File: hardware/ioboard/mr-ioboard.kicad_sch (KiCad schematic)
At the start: 116 parts, among them J1 Conn_01x40_Shielded, J2 USB_C_Receptacle_USB2.0, J3 Conn_01x06, J4 Micro_SD_Card_Det, J5 Conn_01x04, Q1 2N7002, SW1 SW_Push, U1 TPS62822, U10 F1C200S, U2 TPS56637, U3 TPD2E2U06, U4 DS90C363, U5 TPD2E2U06, U6 LD3985M28R_SOT23, U7 TPS62822, U8 FUSB302BMPX, U9 TPD2E2U06, Y1 24MHz

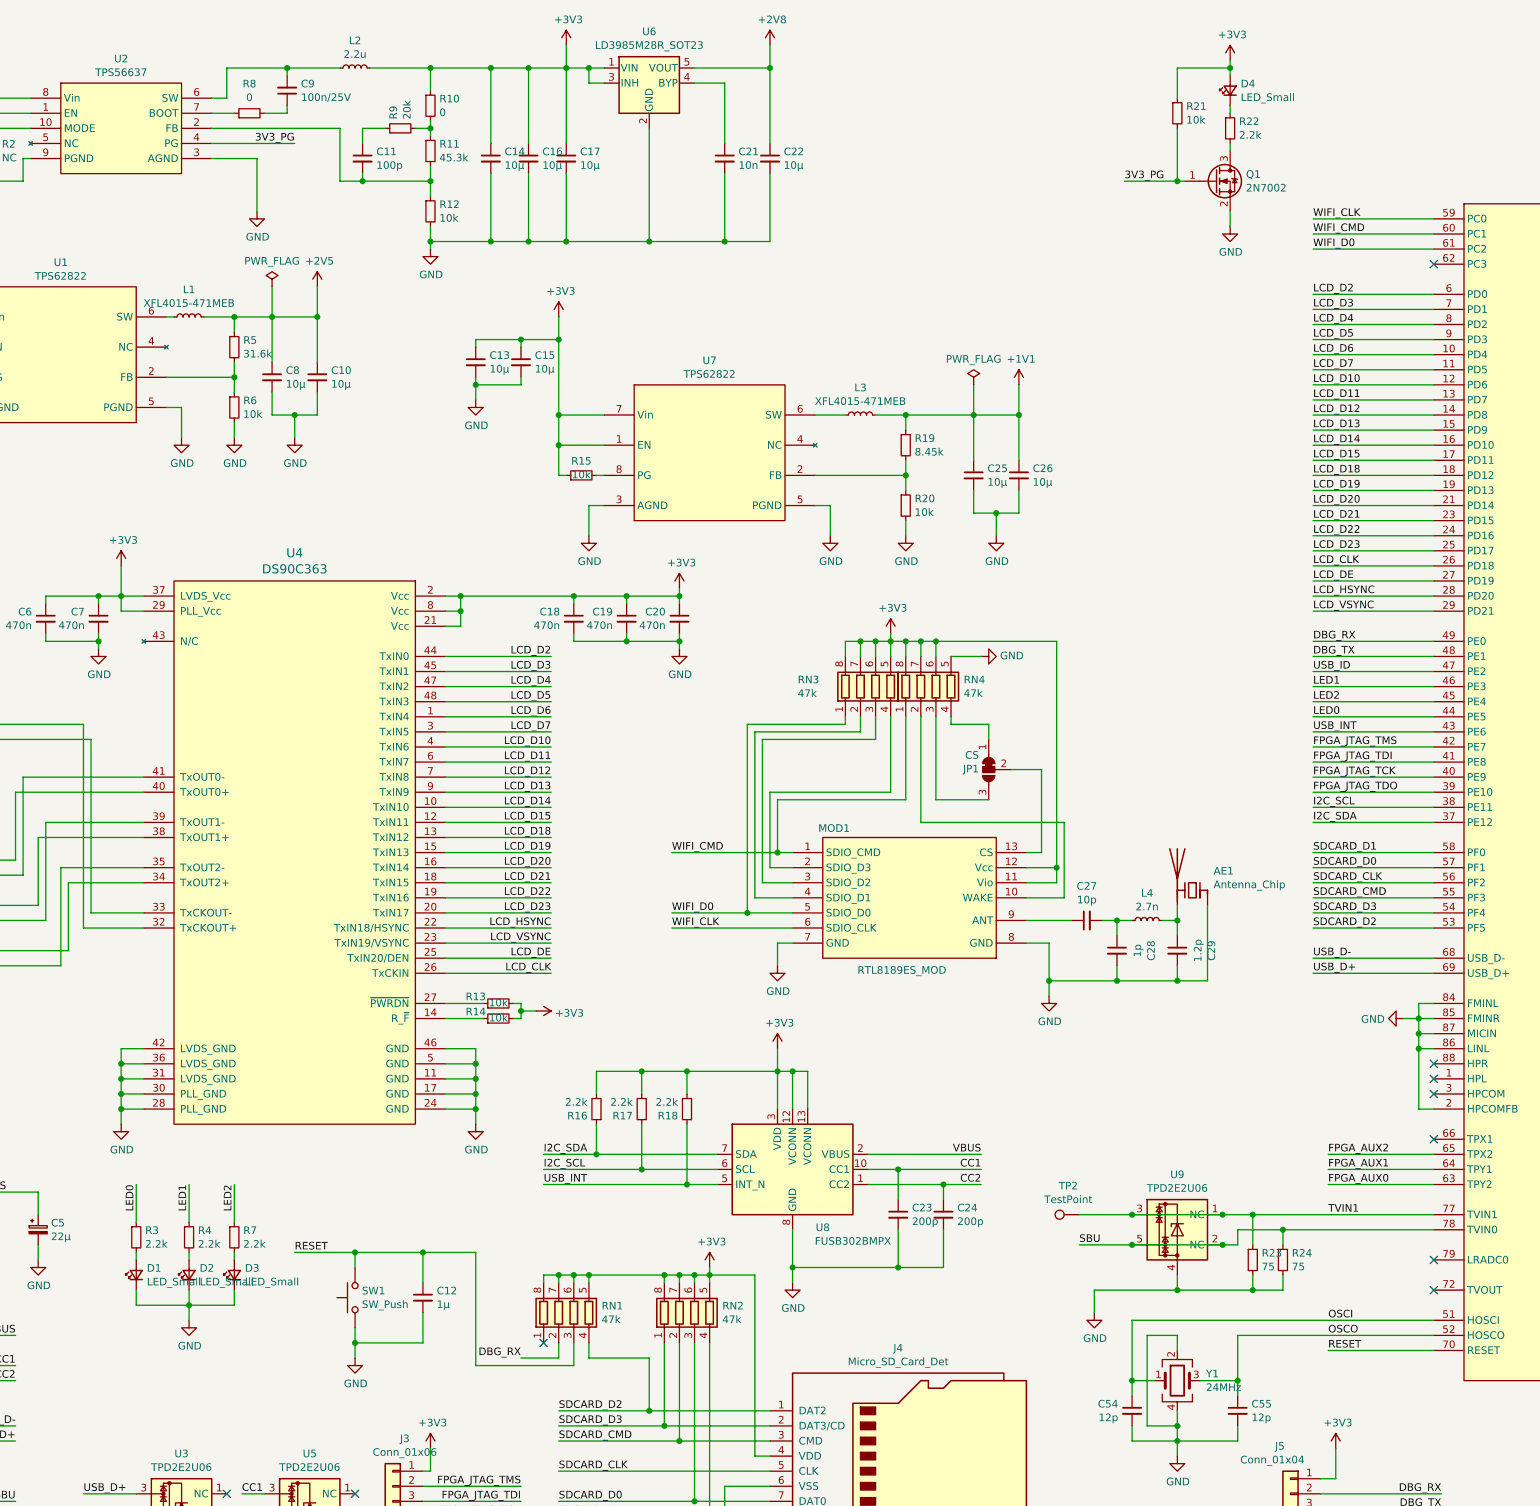
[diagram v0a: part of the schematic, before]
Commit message: Add VLED buck regulator to IO board
Signed-off-by: gatecat <gatecat@ds0.me>
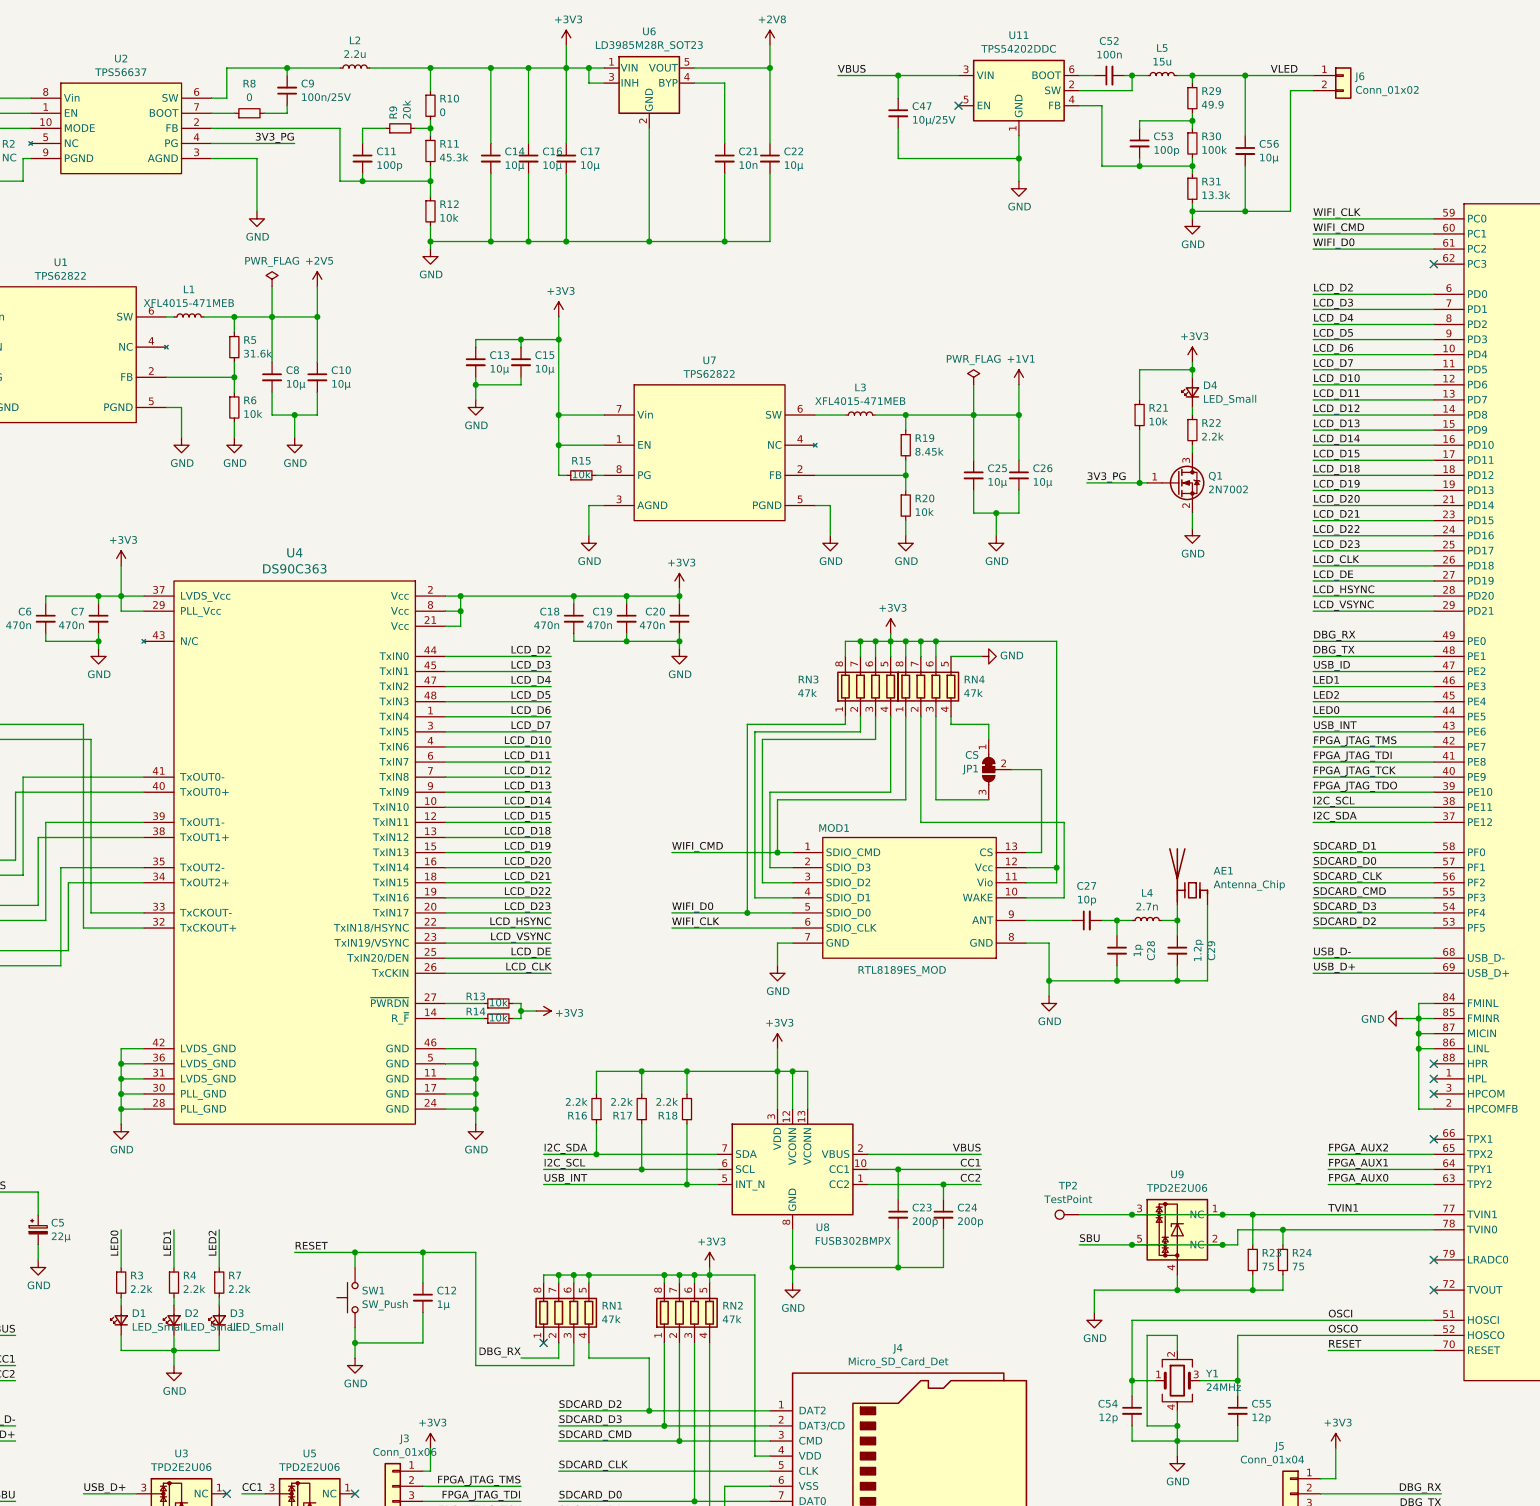
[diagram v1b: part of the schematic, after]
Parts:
- added C47: 10µ/25V, Capacitor_SMD:C_0805_2012Metric, symbol Device:C_Small
- added C52: 100n, Capacitor_SMD:C_0402_1005Metric, symbol Device:C_Small
- added C53: 100p, Capacitor_SMD:C_0402_1005Metric, symbol Device:C_Small
- added C56: 10µ, Capacitor_SMD:C_0805_2012Metric, symbol Device:C_Small
- added J6: Conn_01x02, Connector_PinHeader_2.54mm:PinHeader_1x02_P2.54mm_Vertical, symbol Connector_Generic:Conn_01x02
- added L5: 15u, Inductor_SMD:L_Bourns_SRP7028A_7.3x6.6mm, symbol Device:L_Small
- added R29: 49.9, Resistor_SMD:R_0402_1005Metric, symbol Device:R_Small
- added R30: 100k, Resistor_SMD:R_0402_1005Metric, symbol Device:R_Small
- added R31: 13.3k, Resistor_SMD:R_0402_1005Metric, symbol Device:R_Small
- added U11: TPS54202DDC, Package_TO_SOT_SMD:SOT-23-6, symbol Regulator_Switching:TPS54202DDC
- C54, C55: footprint (none) -> Capacitor_SMD:C_0402_1005Metric
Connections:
- net GND: now also C47.2, C56.2, J6.2 (Pin_2), R31.2, U11.1 (GND)
- net VBUS: now also C47.1, U11.3 (VIN)
- new net: C53.2, R30.2, R31.1, U11.4 (FB)
- new net: C53.1, R29.2, R30.1
- new net: C52.2, L5.1, U11.2 (SW)
- new net: C52.1, U11.6 (BOOT)
- new net VLED: C56.1, J6.1 (Pin_1), L5.2, R29.1
- no-connect marks 21 -> 22
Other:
- moved on the sheet: D1, D2, D3, D4, Q1, R21, R22, R3, R4, R7

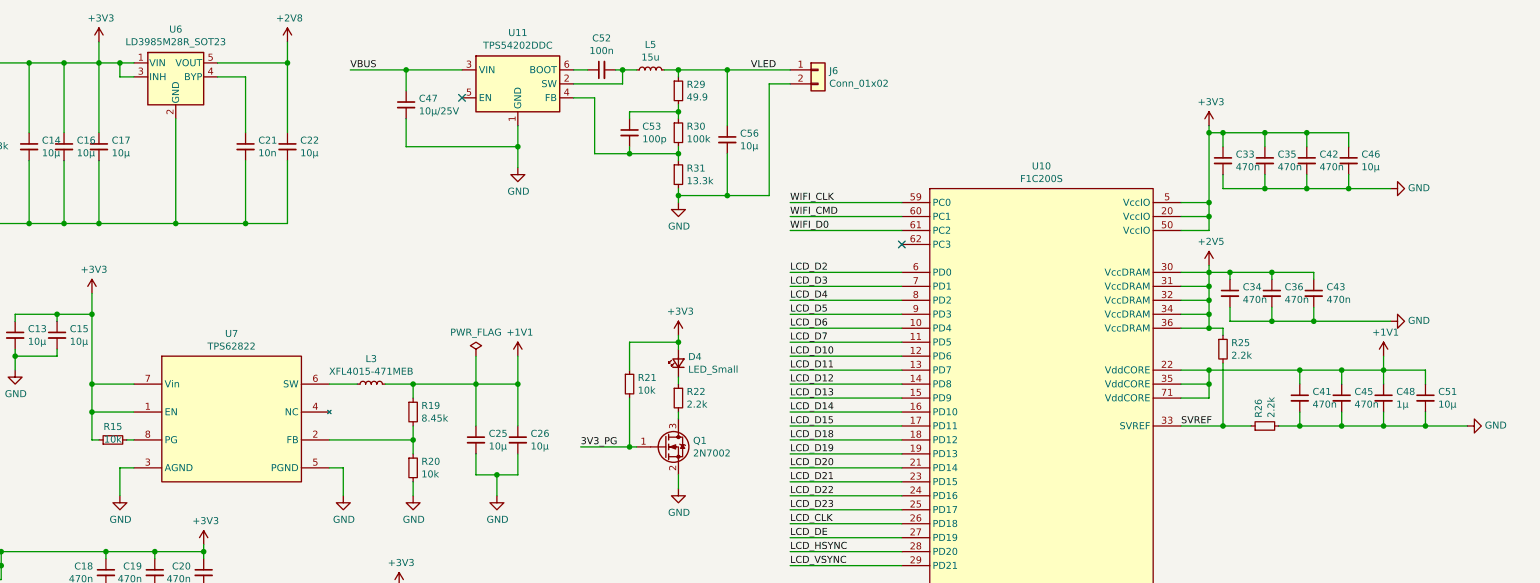
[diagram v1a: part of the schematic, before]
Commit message: Some tidying up of IO board
Signed-off-by: gatecat <gatecat@ds0.me>
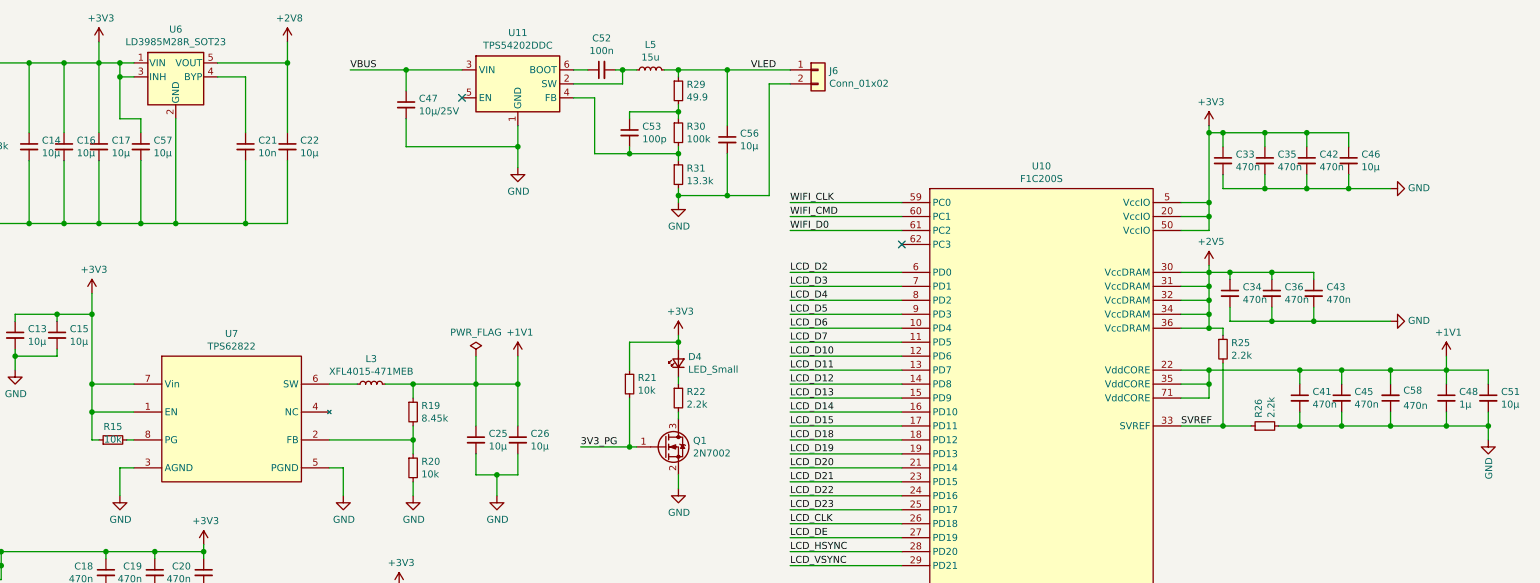
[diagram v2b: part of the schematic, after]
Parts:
- added C57: 10µ, Capacitor_SMD:C_0805_2012Metric, symbol Device:C_Small
- added C58: 470n, Capacitor_SMD:C_0402_1005Metric, symbol Device:C_Small
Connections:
- net +1V1: now also C58.2
- net +3V3: now also C57.1
- net GND: now also C57.2, C58.1
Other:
- moved on the sheet: C48, C51

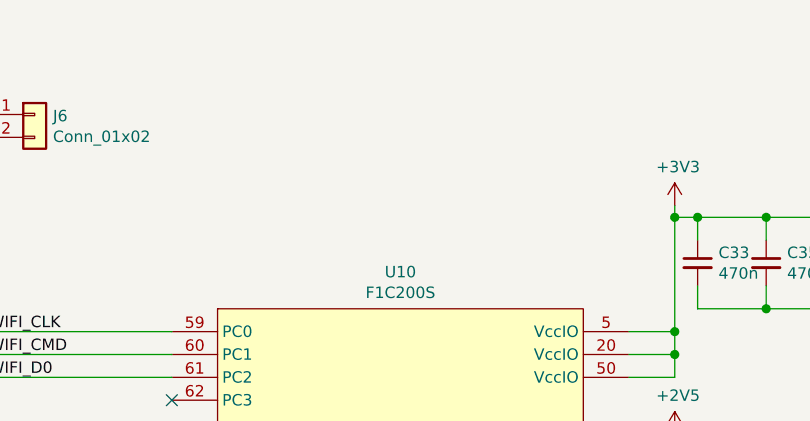
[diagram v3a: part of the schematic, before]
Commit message: Add mounting holes to IO board
Signed-off-by: gatecat <gatecat@ds0.me>
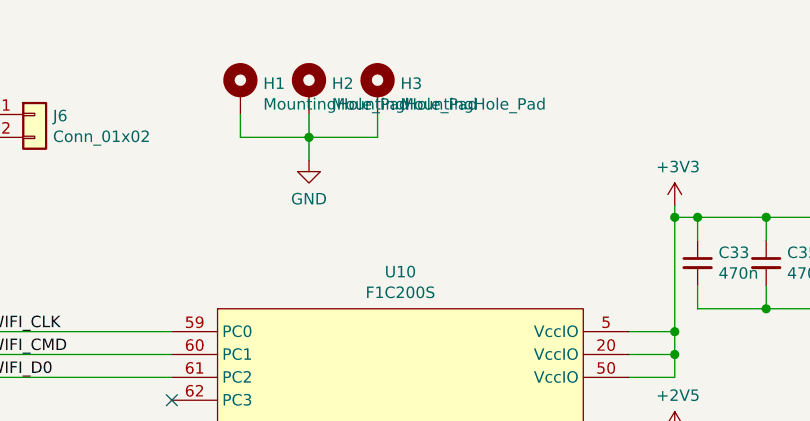
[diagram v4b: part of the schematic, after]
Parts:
- added H1, H2, H3: MountingHole_Pad, MountingHole:MountingHole_3.2mm_M3_Pad_Via, symbol Mechanical:MountingHole_Pad
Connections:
- net GND: now also H1.1, H2.1, H3.1
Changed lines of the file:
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@@
   (junction (at 292.1 186.69) (diameter 1.016) (color 0 0 0 0))
   (junction (at 292.1 189.23) (diameter 1.016) (color 0 0 0 0))
+  (junction (at 309.88 27.94) (diameter 1.016) (color 0 0 0 0))
   (junction (at 347.98 173.99) (diameter 1.016) (color 0 0 0 0))
   (junction (at 347.98 191.77) (diameter 1.016) (color 0 0 0 0))
@@
     (stroke (width 0) (type solid) (color 0 0 0 0))
   )
+  (wire (pts (xy 302.26 25.4) (xy 302.26 27.94))
+    (stroke (width 0) (type solid) (color 0 0 0 0))
+  )
+  (wire (pts (xy 309.88 25.4) (xy 309.88 27.94))
+    (stroke (width 0) (type solid) (color 0 0 0 0))
+  )
+  (wire (pts (xy 309.88 27.94) (xy 302.26 27.94))
+    (stroke (width 0) (type solid) (color 0 0 0 0))
+  )
+  (wire (pts (xy 309.88 27.94) (xy 317.5 27.94))
+    (stroke (width 0) (type solid) (color 0 0 0 0))
+  )
+  (wire (pts (xy 309.88 30.48) (xy 309.88 27.94))
+    (stroke (width 0) (type solid) (color 0 0 0 0))
+  )
+  (wire (pts (xy 317.5 27.94) (xy 317.5 25.4))
+    (stroke (width 0) (type solid) (color 0 0 0 0))
+  )
   (wire (pts (xy 345.44 52.07) (xy 350.52 52.07))
     (stroke (width 0) (type solid) (color 0 0 0 0))
@@
     (pin "1")
   )
+  (symbol (lib_id "power:GND") (at 309.88 30.48 0) (unit 1)
+    (in_bom yes) (on_board yes)
+    (property "Reference" "#PWR0138" (id 0) (at 309.88 36.83 0)
+      (effects (font (size 1.27 1.27)) hide)
+    )
+    (property "Value" "GND" (id 1) (at 309.88 34.8044 0))
+    (property "Footprint" "" (id 2) (at 309.88 30.48 0)
+      (effects (font (size 1.27 1.27)) hide)
+    )
+    (property "Datasheet" "" (id 3) (at 309.88 30.48 0)
+      (effects (font (size 1.27 1.27)) hide)
+    )
+    (pin "1")
+  )
   (symbol (lib_id "power:GND") (at 349.25 243.84 0) (unit 1)
     (in_bom yes) (on_board yes)
@@
     (pin "2")
   )
+  (symbol (lib_id "Mechanical:MountingHole_Pad") (at 302.26 22.86 0) (unit 1)
+    (in_bom yes) (on_board yes)
+    (property "Reference" "H1" (id 0) (at 304.8001 21.9721 0)
+      (effects (font (size 1.27 1.27)) (justify left))
+    )
+    (property "Value" "MountingHole_Pad" (id 1) (at 304.8001 24.2708 0)
+      (effects (font (size 1.27 1.27)) (justify left))
+    )
+    (property "Footprint" "MountingHole:MountingHole_3.2mm_M3_Pad_Via" (id 2) (at 302.26 22.86 0)
+      (effects (font (size 1.27 1.27)) hide)
+    )
+    (property "Datasheet" "~" (id 3) (at 302.26 22.86 0)
+      (effects (font (size 1.27 1.27)) hide)
+    )
+    (pin "1")
+  )
+  (symbol (lib_id "Mechanical:MountingHole_Pad") (at 309.88 22.86 0) (unit 1)
+    (in_bom yes) (on_board yes)
+    (property "Reference" "H2" (id 0) (at 312.4201 21.9721 0)
+      (effects (font (size 1.27 1.27)) (justify left))
+    )
+    (property "Value" "MountingHole_Pad" (id 1) (at 312.4201 24.2708 0)
+      (effects (font (size 1.27 1.27)) (justify left))
+    )
+    (property "Footprint" "MountingHole:MountingHole_3.2mm_M3_Pad_Via" (id 2) (at 309.88 22.86 0)
+      (effects (font (size 1.27 1.27)) hide)
+    )
+    (property "Datasheet" "~" (id 3) (at 309.88 22.86 0)
+      (effects (font (size 1.27 1.27)) hide)
+    )
+    (pin "1")
+  )
+  (symbol (lib_id "Mechanical:MountingHole_Pad") (at 317.5 22.86 0) (unit 1)
+    (in_bom yes) (on_board yes)
+    (property "Reference" "H3" (id 0) (at 320.0401 21.9721 0)
+      (effects (font (size 1.27 1.27)) (justify left))
+    )
+    (property "Value" "MountingHole_Pad" (id 1) (at 320.0401 24.2708 0)
+      (effects (font (size 1.27 1.27)) (justify left))
+    )
+    (property "Footprint" "MountingHole:MountingHole_3.2mm_M3_Pad_Via" (id 2) (at 317.5 22.86 0)
+      (effects (font (size 1.27 1.27)) hide)
+    )
+    (property "Datasheet" "~" (id 3) (at 317.5 22.86 0)
+      (effects (font (size 1.27 1.27)) hide)
+    )
+    (pin "1")
+  )
   (symbol (lib_id "Connector_Generic:Conn_01x02") (at 279.4 25.4 0) (unit 1)
     (in_bom yes) (on_board yes)
@@
       (reference "#PWR0137") (unit 1) (value "GND") (footprint "")
     )
+    (path "/b95e3e05-4846-4ea9-b2cd-32264b6cbefc"
+      (reference "#PWR0138") (unit 1) (value "GND") (footprint "")
+    )
     (path "/d4f90935-3bb7-4ac9-9306-54ace2c6fe85"
       (reference "#PWR0139") (unit 1) (value "+2V5") (footprint "")
@@
       (reference "FB1") (unit 1) (value "FerriteBead_Small") (footprint "Inductor_SMD:L_0603_1608Metric")
     )
+    (path "/3256fef0-1761-4fe8-a7c7-a32266735f2e"
+      (reference "H1") (unit 1) (value "MountingHole_Pad") (footprint "MountingHole:MountingHole_3.2mm_M3_Pad_Via")
+    )
+    (path "/4496ac33-77a9-4f08-9518-9dd55d872732"
+      (reference "H2") (unit 1) (value "MountingHole_Pad") (footprint "MountingHole:MountingHole_3.2mm_M3_Pad_Via")
+    )
+    (path "/f91649ca-aaa9-4ce8-8588-97015c0f8623"
+      (reference "H3") (unit 1) (value "MountingHole_Pad") (footprint "MountingHole:MountingHole_3.2mm_M3_Pad_Via")
+    )
     (path "/a987a61e-0ab1-4aee-b63b-0b9b74fb10fe"
